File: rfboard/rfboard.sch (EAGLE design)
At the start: 31 parts, among them U1 MAX1555

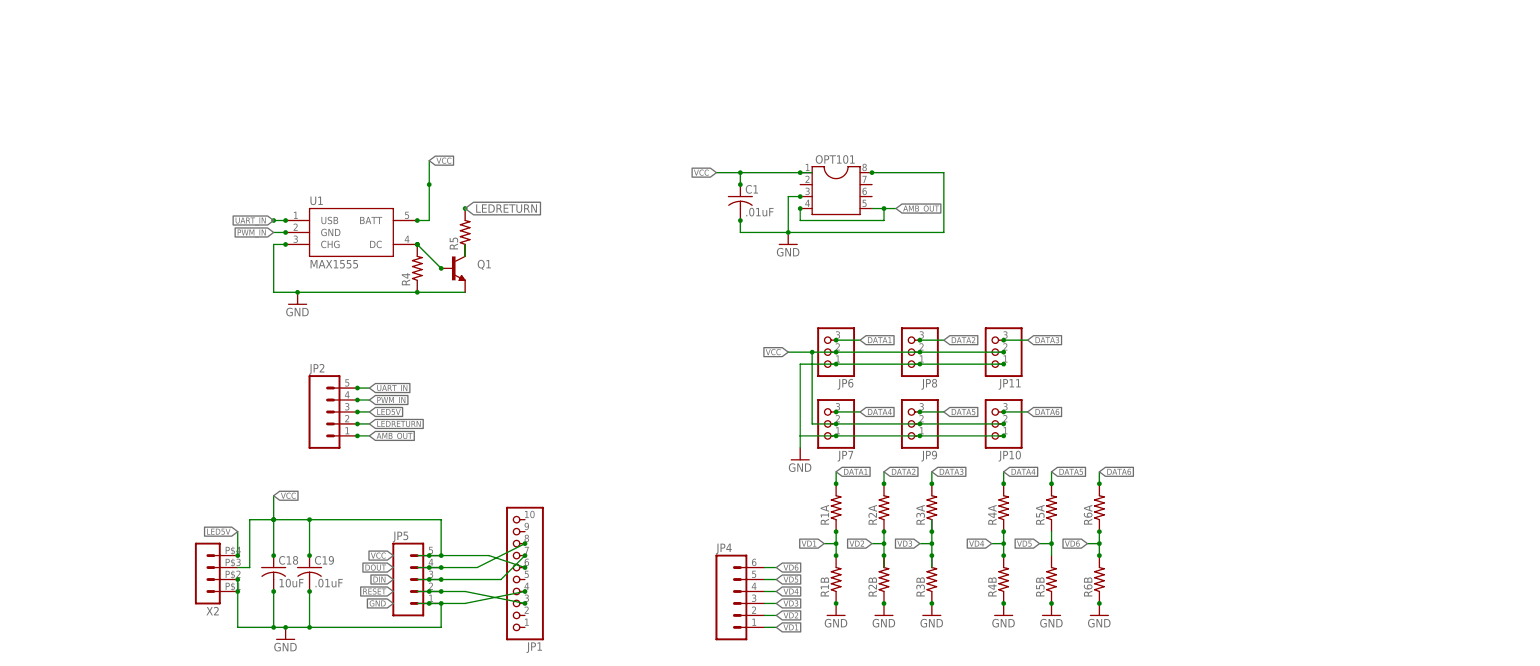
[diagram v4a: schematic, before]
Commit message: changing XBee pinout, and adding logic converters
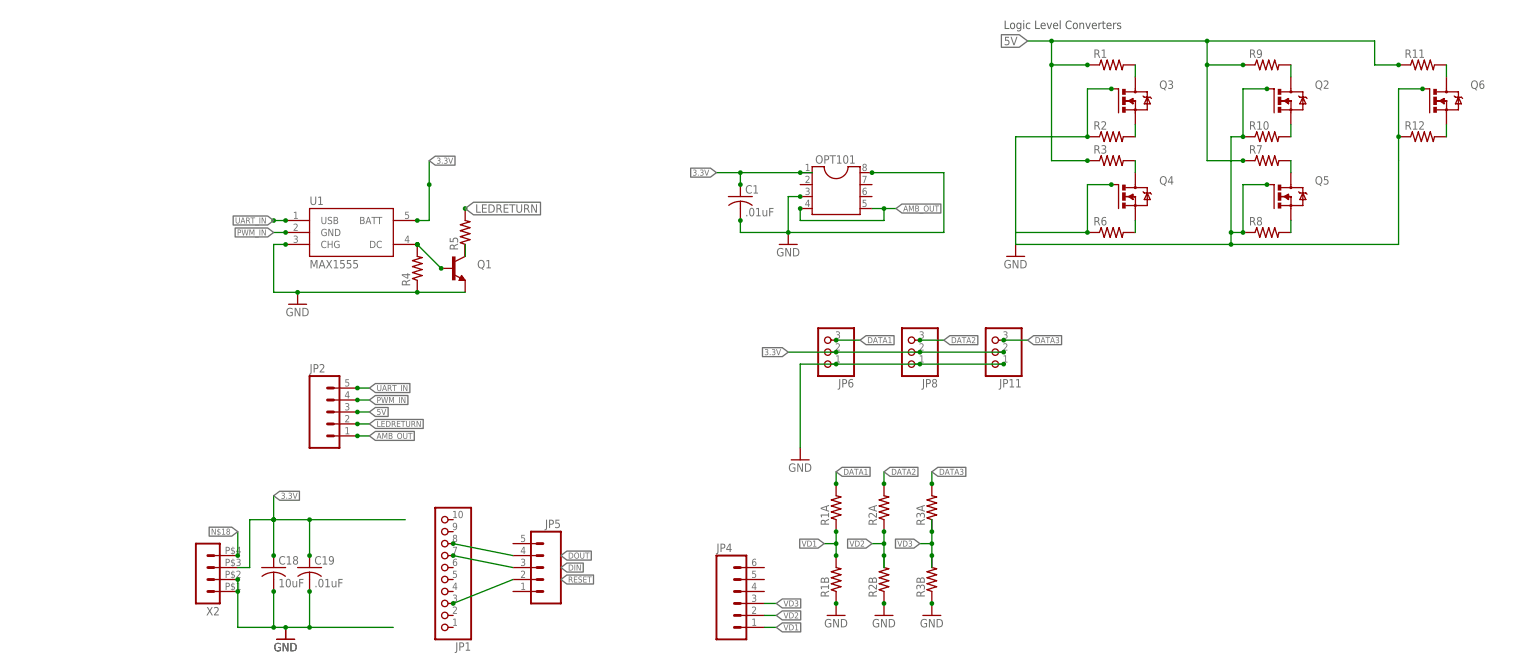
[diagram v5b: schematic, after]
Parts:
- removed JP10, JP7, JP9: (no value), pinhead-2:PINHD-1X03_2.00
- removed R4A, R4B, R5A, R5B, R6A, R6B: (no value), rcl:R-US_R1206
- added Q2, Q3, Q4, Q5, Q6: IRLML5203, ngohara_parts:IRLML5203
- added R1, R10, R11, R12, R2, R3, R6, R7, R8, R9: (no value), resistor:R-US_R0805
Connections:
- removed net DATA4: JP7.3, R4A.2
- removed net DATA5: JP9.3, R5A.2
- removed net DATA6: JP10.3, R6A.2
- removed net LED5V: JP2.3, X2.4
- removed net VCC: C1.1, C18.1, C19.1, JP1.6, JP10.2, JP11.2, JP5.5, JP6.2, JP7.2, JP8.2, JP9.2, OPT101.1, U1.BATT, X2.3
- removed net VD4: JP4.4, R4A.1, R4B.2
- removed net VD5: JP4.5, R5A.1, R5B.2
- removed net VD6: JP4.6, R6A.1, R6B.2
- new net 3.3V: C1.1, C18.1, C19.1, JP11.2, JP6.2, JP8.2, OPT101.1, U1.BATT, X2.3
- new net 5V: JP2.3, R1.1, R11.1, R3.1, R7.1, R9.1
- new net N$1: Q4.D, R3.2
- new net N$10: Q5.S, R8.2
- new net N$11: Q6.S, R12.2
- new net N$12: Q6.D, R11.2
- new net N$18: X2.4
- new net N$2: Q4.S, R6.2
- new net N$4: Q3.S, R2.2
- new net N$6: Q3.D, R1.2
- new net N$7: Q2.D, R9.2
- new net N$8: Q2.S, R10.2
- new net N$9: Q5.D, R7.2
- net GND: now also Q2.G, Q3.G, Q4.G, Q5.G, Q6.G, R10.1, R12.1, R2.1, R6.1, R8.1; no longer JP1.4, JP10.1, JP5.1, JP7.1, JP9.1, R4B.1, R5B.1, R6B.1
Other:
- note added: "Logic Level Converters"
- moved on the sheet: JP1, JP5

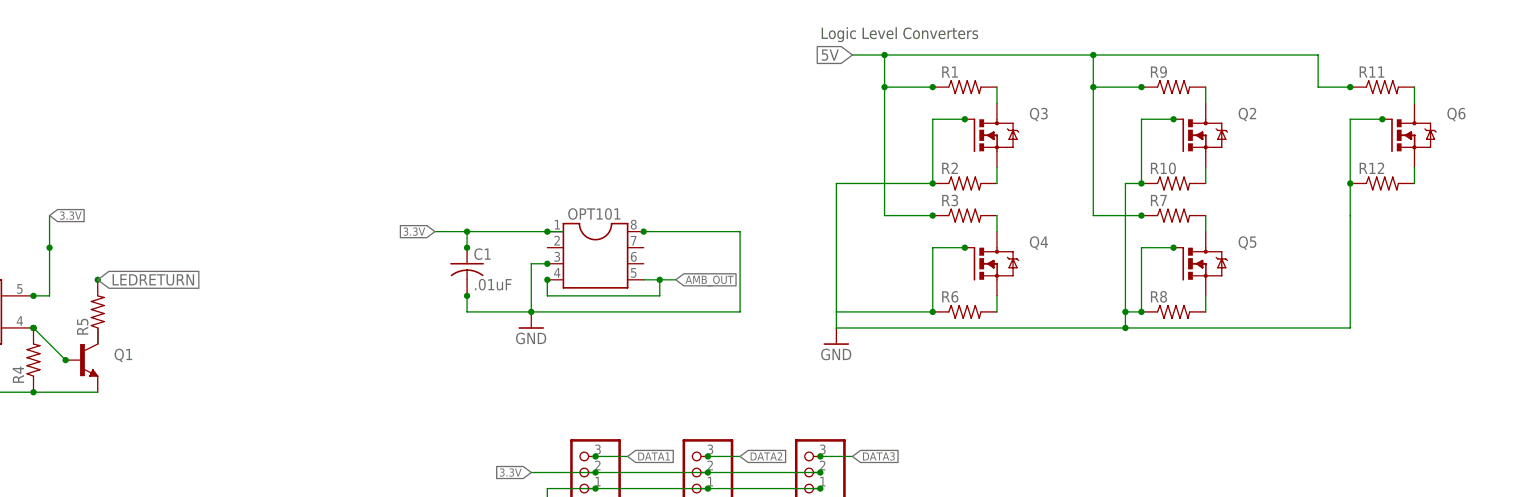
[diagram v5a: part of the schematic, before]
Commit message: changing logic converters and pinout
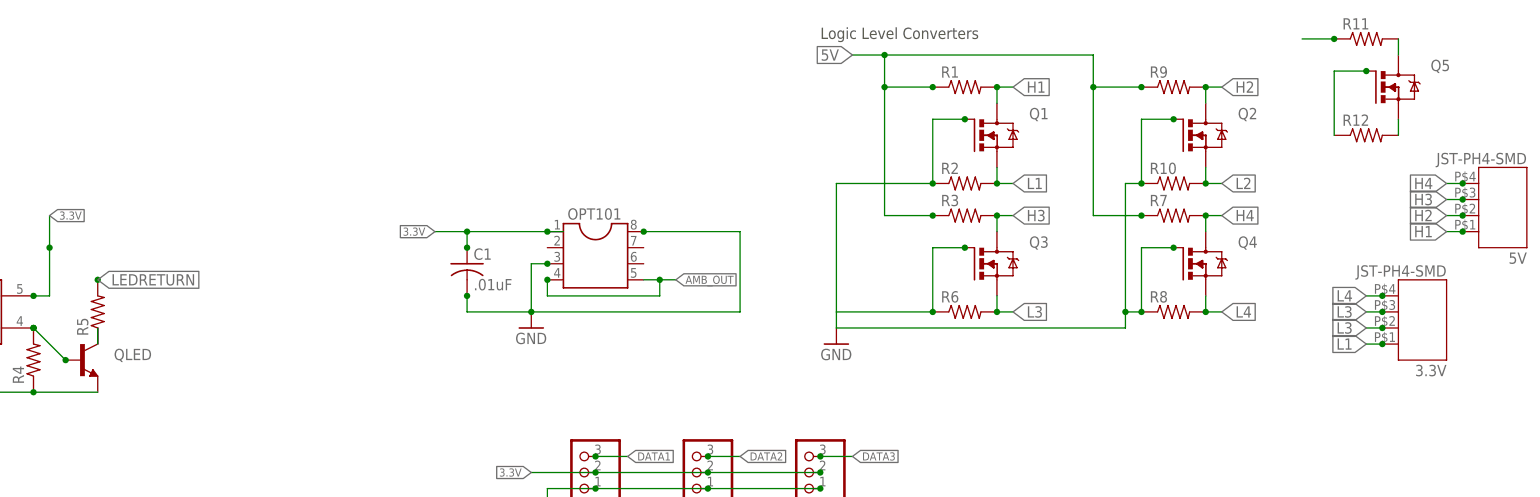
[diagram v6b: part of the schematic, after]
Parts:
- removed Q6: IRLML5203, ngohara_parts:IRLML5203
- added 3.3V, 5V: JST-PH4-SMD, jst-ph:JST-PH4-SMD
- added QLED: (no value), SparkFun-DiscreteSemi:TRANSISTOR_NPN"
- Q1: value (none) -> IRLML5203; device SparkFun-DiscreteSemi:TRANSISTOR_NPN" -> ngohara_parts:IRLML5203
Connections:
- removed net N$1: Q4.D, R3.2
- removed net N$10: Q5.S, R8.2
- removed net N$2: Q4.S, R6.2
- removed net N$4: Q3.S, R2.2
- removed net N$6: Q3.D, R1.2
- removed net N$7: Q2.D, R9.2
- removed net N$8: Q2.S, R10.2
- removed net N$9: Q5.D, R7.2
- new net H1: 5V.1, Q1.D, R1.2
- new net H2: 5V.2, Q2.D, R9.2
- new net H3: 5V.3, Q3.D, R3.2
- new net H4: 5V.4, Q4.D, R7.2
- new net L1: 3.3V.1, Q1.S, R2.2
- new net L2: 3.3V.2, Q2.S, R10.2
- new net L3: 3.3V.3, Q3.S, R6.2
- new net L4: 3.3V.4, Q4.S, R8.2
- new net N$13: R11.1
- new net N$14: Q5.G, R12.1
- net 5V: no longer R11.1
- net GND: now also Q1.G, QLED.E; no longer Q1.E, Q5.G, Q6.G, R12.1
- net N$11: now also Q5.S; no longer Q6.S
- net N$12: now also Q5.D; no longer Q6.D
- net N$3: now also QLED.B; no longer Q1.B
- net N$5: now also QLED.C; no longer Q1.C
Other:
- note removed: "And Gate Circuit"
- moved on the sheet: Q3, Q4, Q5, R11, R12

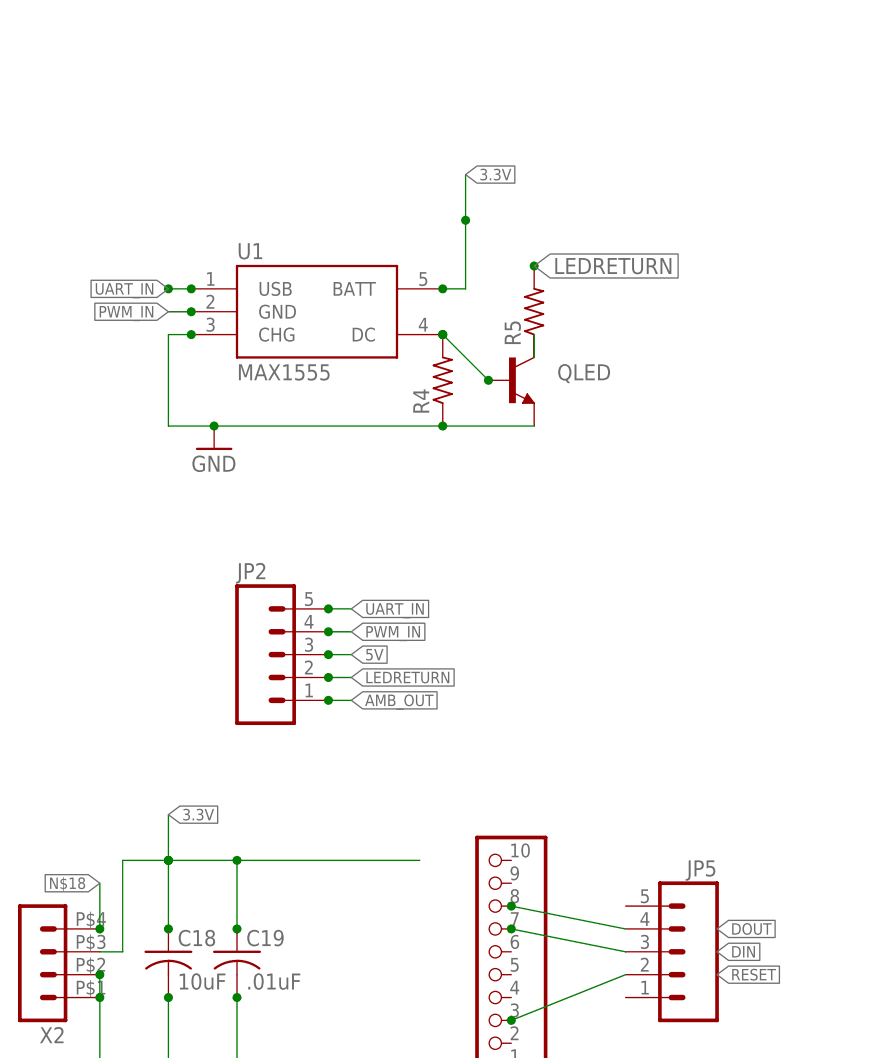
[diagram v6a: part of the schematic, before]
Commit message: deleted AND circuit from RF board
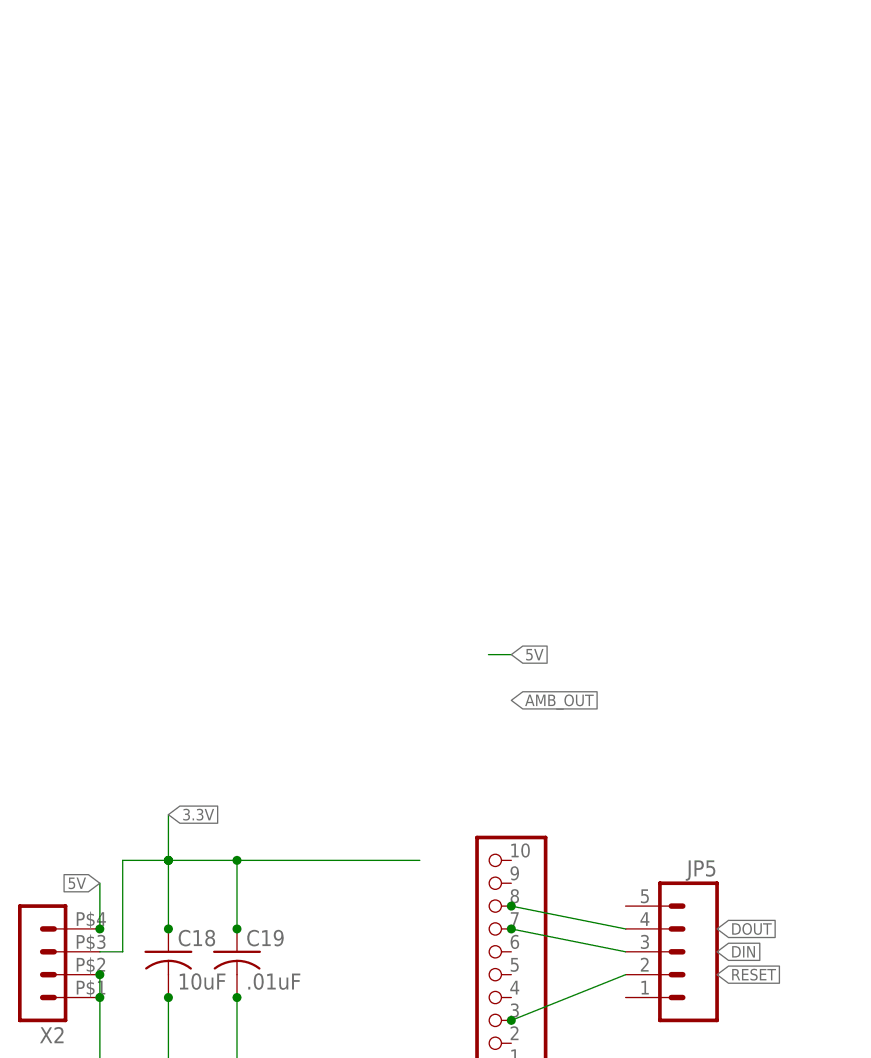
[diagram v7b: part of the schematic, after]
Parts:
- removed JP2: (no value), SparkFun-Connectors:M05LOCK
- removed QLED: (no value), SparkFun-DiscreteSemi:TRANSISTOR_NPN"
- removed R4, R5: (no value), rcl:R-US_R1206
- removed U1: MAX1555, SparkFun-PowerIC:MAX1555
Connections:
- removed net LEDRETURN: JP2.2, R5.2
- removed net N$18: X2.4
- removed net N$3: QLED.B, R4.2, U1.DC
- removed net N$5: QLED.C, R5.1
- removed net PWM_IN: JP2.4, U1.GND
- removed net UART_IN: JP2.5, U1.USB
- net 3.3V: no longer U1.BATT
- net 5V: now also X2.4; no longer JP2.3
- net AMB_OUT: no longer JP2.1
- net GND: no longer QLED.E, R4.1, U1.CHG
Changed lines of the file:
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@@
 <part name="C18" library="rcl" deviceset="C-US" device="C1206K" value="10uF"/>
 <part name="C19" library="rcl" deviceset="C-US" device="C0805K" value=".01uF"/>
-<part name="QLED" library="SparkFun-DiscreteSemi" deviceset="TRANSISTOR_NPN" device="&quot;"/>
-<part name="U1" library="SparkFun-PowerIC" deviceset="MAX1555" device=""/>
-<part name="R5" library="rcl" deviceset="R-US_" device="R1206"/>
 <part name="X2" library="con-molex-micro-fit-3_0" deviceset="HEADER_POS4_?" device="43045-0406"/>
-<part name="R4" library="rcl" deviceset="R-US_" device="R1206"/>
 <part name="R1A" library="rcl" deviceset="R-US_" device="R1206"/>
 <part name="R2A" library="rcl" deviceset="R-US_" device="R1206"/>
@@
 <part name="JP11" library="pinhead-2" deviceset="PINHD-1X03" device="_2.00"/>
 <part name="GND8" library="supply1" deviceset="GND" device=""/>
-<part name="GND9" library="supply1" deviceset="GND" device=""/>
 <part name="C1" library="rcl" deviceset="C-US" device="C0805K" value=".01uF"/>
 <part name="GND10" library="supply1" deviceset="GND" device=""/>
 <part name="JP1" library="pinhead-2" deviceset="PINHD-1X10" device="_2.00"/>
-<part name="JP2" library="SparkFun-Connectors" deviceset="M05" device="LOCK"/>
 <part name="Q2" library="ngohara_parts" deviceset="IRLML5203" device=""/>
 <part name="Q1" library="ngohara_parts" deviceset="IRLML5203" device=""/>
@@
 <plain>
 <text x="134.62" y="134.62" size="1.27" layer="121">This is the Ambient light sensor</text>
-<wire x1="15.24" y1="137.16" x2="96.52" y2="137.16" width="0.1524" layer="121"/>
-<wire x1="96.52" y1="137.16" x2="96.52" y2="86.36" width="0.1524" layer="121"/>
-<wire x1="96.52" y1="86.36" x2="15.24" y2="86.36" width="0.1524" layer="121"/>
-<wire x1="15.24" y1="86.36" x2="15.24" y2="137.16" width="0.1524" layer="121"/>
 <wire x1="12.7" y1="63.5" x2="104.14" y2="63.5" width="0.1524" layer="121"/>
 <wire x1="104.14" y1="63.5" x2="104.14" y2="12.7" width="0.1524" layer="121"/>
@@
 <instance part="C18" gate="G$1" x="33.02" y="40.64"/>
 <instance part="C19" gate="G$1" x="40.64" y="40.64"/>
-<instance part="QLED" gate="G$1" x="71.12" y="104.14"/>
-<instance part="U1" gate="G$1" x="50.8" y="111.76"/>
-<instance part="R5" gate="G$1" x="73.66" y="111.76" rot="R90"/>
 <instance part="X2" gate="G$1" x="20.32" y="40.64" rot="R180"/>
-<instance part="R4" gate="G$1" x="63.5" y="104.14" rot="R90"/>
 <instance part="R1A" gate="G$1" x="152.4" y="53.34" rot="R90"/>
 <instance part="R2A" gate="G$1" x="162.56" y="53.34" rot="R90"/>
@@
 <instance part="JP11" gate="A" x="185.42" y="86.36" rot="R180"/>
 <instance part="GND8" gate="1" x="144.78" y="63.5"/>
-<instance part="GND9" gate="1" x="38.1" y="96.52"/>
 <instance part="C1" gate="G$1" x="132.08" y="119.38"/>
 <instance part="GND10" gate="1" x="142.24" y="109.22"/>
 <instance part="JP1" gate="A" x="68.58" y="38.1" rot="R180"/>
-<instance part="JP2" gate="G$1" x="43.18" y="73.66"/>
 <instance part="Q2" gate="G$1" x="246.38" y="139.7" smashed="yes">
 <attribute name="NAME" x="254" y="142.24" size="1.778" layer="95"/>
@@
 </segment>
 </net>
-<net name="N$3" class="0">
-<segment>
-<pinref part="U1" gate="G$1" pin="DC"/>
-<pinref part="QLED" gate="G$1" pin="B"/>
-<wire x1="63.5" y1="109.22" x2="68.58" y2="104.14" width="0.1524" layer="91"/>
-<junction x="63.5" y="109.22"/>
-<junction x="68.58" y="104.14"/>
-<pinref part="R4" gate="G$1" pin="2"/>
-<junction x="63.5" y="109.22"/>
-</segment>
-</net>
-<net name="N$5" class="0">
-<segment>
-<pinref part="QLED" gate="G$1" pin="C"/>
-<pinref part="R5" gate="G$1" pin="1"/>
-<wire x1="73.66" y1="109.22" x2="73.66" y2="106.68" width="0.1524" layer="91"/>
-</segment>
-</net>
 <net name="GND" class="0">
-<segment>
-<pinref part="U1" gate="G$1" pin="CHG"/>
-<junction x="35.56" y="109.22"/>
-<wire x1="35.56" y1="109.22" x2="33.02" y2="109.22" width="0.1524" layer="91"/>
-<wire x1="33.02" y1="109.22" x2="33.02" y2="99.06" width="0.1524" layer="91"/>
-<pinref part="QLED" gate="G$1" pin="E"/>
-<wire x1="73.66" y1="99.06" x2="63.5" y2="99.06" width="0.1524" layer="91"/>
-<pinref part="R4" gate="G$1" pin="1"/>
-<junction x="63.5" y="99.06"/>
-<wire x1="63.5" y1="99.06" x2="38.1" y2="99.06" width="0.1524" layer="91"/>
-<pinref part="GND9" gate="1" pin="GND"/>
-<junction x="38.1" y="99.06"/>
-<wire x1="38.1" y1="99.06" x2="33.02" y2="99.06" width="0.1524" layer="91"/>
-</segment>
 <segment>
 <wire x1="40.64" y1="27.94" x2="35.56" y2="27.94" width="0.1524" layer="91"/>
@@
 </segment>
 </net>
-<net name="UART_IN" class="0">
-<segment>
-<label x="33.02" y="114.3" size="1.27" layer="95" rot="R180" xref="yes"/>
-<pinref part="U1" gate="G$1" pin="USB"/>
-<junction x="35.56" y="114.3"/>
-<junction x="33.02" y="114.3"/>
-<wire x1="33.02" y1="114.3" x2="35.56" y2="114.3" width="0.1524" layer="91"/>
-</segment>
-<segment>
-<wire x1="50.8" y1="78.74" x2="53.34" y2="78.74" width="0.1524" layer="91"/>
-<label x="53.34" y="78.74" size="1.27" layer="95" xref="yes"/>
-<pinref part="JP2" gate="G$1" pin="5"/>
-<junction x="50.8" y="78.74"/>
-</segment>
-</net>
-<net name="PWM_IN" class="0">
-<segment>
-<label x="33.02" y="111.76" size="1.27" layer="95" rot="R180" xref="yes"/>
-<pinref part="U1" gate="G$1" pin="GND"/>
-<wire x1="33.02" y1="111.76" x2="35.56" y2="111.76" width="0.1524" layer="91"/>
-<junction x="35.56" y="111.76"/>
-</segment>
-<segment>
-<wire x1="50.8" y1="76.2" x2="53.34" y2="76.2" width="0.1524" layer="91"/>
-<label x="53.34" y="76.2" size="1.27" layer="95" xref="yes"/>
-<pinref part="JP2" gate="G$1" pin="4"/>
-<junction x="50.8" y="76.2"/>
-</segment>
-</net>
-<net name="LEDRETURN" class="0">
-<segment>
-<pinref part="R5" gate="G$1" pin="2"/>
-<junction x="73.66" y="116.84"/>
-<label x="73.66" y="116.84" size="1.778" layer="95" xref="yes"/>
-</segment>
-<segment>
-<wire x1="50.8" y1="71.12" x2="53.34" y2="71.12" width="0.1524" layer="91"/>
-<label x="53.34" y="71.12" size="1.27" layer="95" xref="yes"/>
-<pinref part="JP2" gate="G$1" pin="2"/>
-<junction x="50.8" y="71.12"/>
-</segment>
-</net>
 <net name="VD3" class="0">
 <segment>
@@
 <label x="165.1" y="116.84" size="1.27" layer="95" xref="yes"/>
 <junction x="144.78" y="116.84"/>
-<wire x1="53.34" y1="68.58" x2="50.8" y2="68.58" width="0.1524" layer="91"/>
-<pinref part="JP2" gate="G$1" pin="1"/>
-<junction x="50.8" y="68.58"/>
-<label x="53.34" y="68.58" size="1.27" layer="95" xref="yes"/>
+<label x="71.12" y="68.58" size="1.27" layer="95" xref="yes"/>
 </segment>
 </net>
@@
 <junction x="132.08" y="121.92"/>
 <label x="127" y="124.46" size="1.27" layer="95" rot="R180" xref="yes"/>
-</segment>
-<segment>
-<junction x="66.04" y="121.92"/>
-<wire x1="66.04" y1="127" x2="66.04" y2="121.92" width="0.1524" layer="91"/>
-<wire x1="66.04" y1="114.3" x2="66.04" y2="121.92" width="0.1524" layer="91"/>
-<pinref part="U1" gate="G$1" pin="BATT"/>
-<junction x="63.5" y="114.3"/>
-<wire x1="63.5" y1="114.3" x2="66.04" y2="114.3" width="0.1524" layer="91"/>
-<label x="66.04" y="127" size="1.27" layer="95" xref="yes"/>
 </segment>
 </net>
@@
 </segment>
 <segment>
-<wire x1="50.8" y1="73.66" x2="53.34" y2="73.66" width="0.1524" layer="91"/>
-<label x="53.34" y="73.66" size="1.27" layer="95" xref="yes"/>
-<pinref part="JP2" gate="G$1" pin="3"/>
-<junction x="50.8" y="73.66"/>
-</segment>
-</net>
-<net name="N$18" class="0">
+<wire x1="68.58" y1="73.66" x2="71.12" y2="73.66" width="0.1524" layer="91"/>
+<label x="71.12" y="73.66" size="1.27" layer="95" xref="yes"/>
+</segment>
 <segment>
 <pinref part="X2" gate="G$1" pin="4"/>
